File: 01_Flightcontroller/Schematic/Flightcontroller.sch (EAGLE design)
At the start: 86 parts, among them IC1 FT232RL, IC2 MPU6000, IC3 BMP280, J1 2908-05WB-MG, U1 STM32F7X2RXT, U2 ATMEGA328P_TQFP, U3 LM3940IMPX-3.3/NOPB, U4 TXB0104, Y1 8MHz, Y2 16MHz

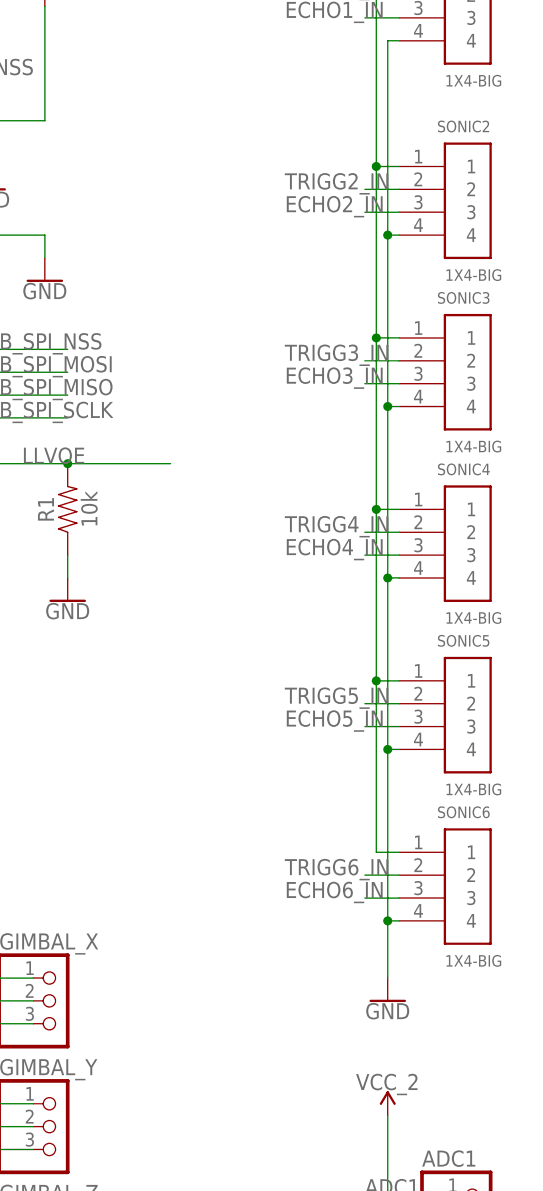
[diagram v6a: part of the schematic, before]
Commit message: Löschen von ünnötigen Pins
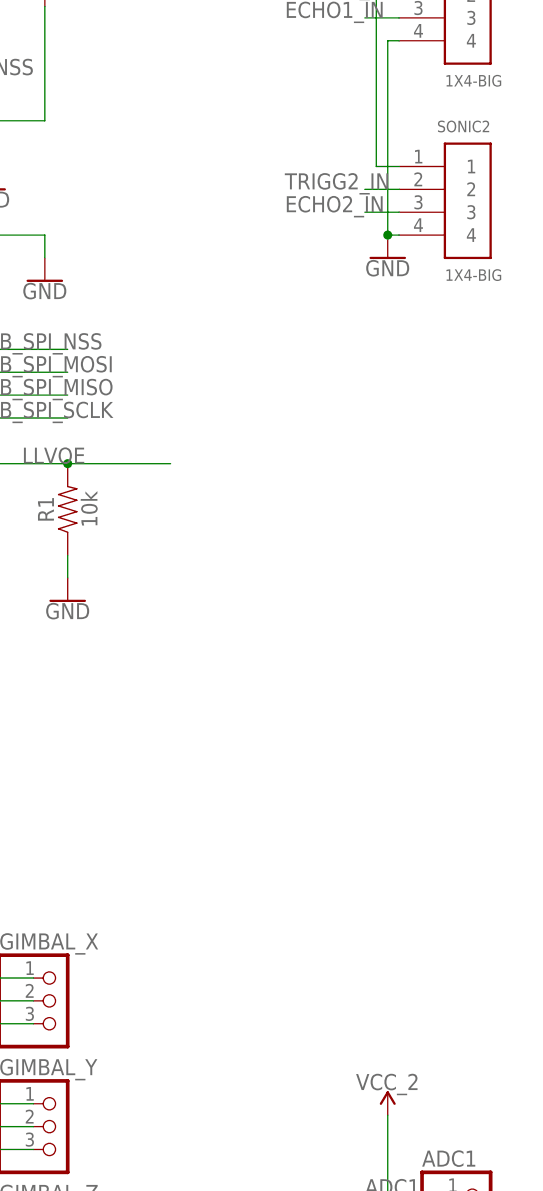
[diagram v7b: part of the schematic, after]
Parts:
- removed SONIC3, SONIC4, SONIC5, SONIC6: 1X4-BIG, adafruit:1X4-BIG
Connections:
- net ECHO3_IN: no longer SONIC3.3
- net ECHO4_IN: no longer SONIC4.3
- net ECHO5_IN: no longer SONIC5.3
- net ECHO6_IN: no longer SONIC6.3
- net GND: no longer SONIC3.4, SONIC4.4, SONIC5.4, SONIC6.4
- net TRIGG3_IN: no longer SONIC3.2
- net TRIGG4_IN: no longer SONIC4.2
- net TRIGG5_IN: no longer SONIC5.2
- net TRIGG6_IN: no longer SONIC6.2
- net VCC_2: no longer SONIC3.1, SONIC4.1, SONIC5.1, SONIC6.1
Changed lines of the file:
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@@
 <?xml version="1.0" encoding="utf-8"?>
 <!DOCTYPE eagle SYSTEM "eagle.dtd">
-<eagle version="9.3.2">
+<eagle version="9.1.3">
 <drawing>
 <settings>
@@
 <part name="SONIC1" library="adafruit" library_urn="urn:adsk.eagle:library:420" deviceset="1X4" device="-BIG" package3d_urn="urn:adsk.eagle:package:6240658/1"/>
 <part name="SONIC2" library="adafruit" library_urn="urn:adsk.eagle:library:420" deviceset="1X4" device="-BIG" package3d_urn="urn:adsk.eagle:package:6240658/1"/>
-<part name="SONIC3" library="adafruit" library_urn="urn:adsk.eagle:library:420" deviceset="1X4" device="-BIG" package3d_urn="urn:adsk.eagle:package:6240658/1"/>
-<part name="SONIC4" library="adafruit" library_urn="urn:adsk.eagle:library:420" deviceset="1X4" device="-BIG" package3d_urn="urn:adsk.eagle:package:6240658/1"/>
-<part name="SONIC5" library="adafruit" library_urn="urn:adsk.eagle:library:420" deviceset="1X4" device="-BIG" package3d_urn="urn:adsk.eagle:package:6240658/1"/>
-<part name="SONIC6" library="adafruit" library_urn="urn:adsk.eagle:library:420" deviceset="1X4" device="-BIG" package3d_urn="urn:adsk.eagle:package:6240658/1"/>
 <part name="SUPPLY22" library="SparkFun-PowerSymbols" library_urn="urn:adsk.eagle:library:530" deviceset="VCC_2" device=""/>
 <part name="GND21" library="SparkFun-PowerSymbols" library_urn="urn:adsk.eagle:library:530" deviceset="GND" device=""/>
@@
 <attribute name="VALUE" x="369.57" y="40.64" size="1.27" layer="96" font="vector"/>
 </instance>
-<instance part="SONIC3" gate="G$1" x="369.57" y="31.75" smashed="yes">
-<attribute name="NAME" x="374.65" y="39.37" size="1.27" layer="95" font="vector" rot="R180"/>
-<attribute name="VALUE" x="369.57" y="21.59" size="1.27" layer="96" font="vector"/>
-</instance>
-<instance part="SONIC4" gate="G$1" x="369.57" y="12.7" smashed="yes">
-<attribute name="NAME" x="374.65" y="20.32" size="1.27" layer="95" font="vector" rot="R180"/>
-<attribute name="VALUE" x="369.57" y="2.54" size="1.27" layer="96" font="vector"/>
-</instance>
-<instance part="SONIC5" gate="G$1" x="369.57" y="-6.35" smashed="yes">
-<attribute name="NAME" x="374.65" y="1.27" size="1.27" layer="95" font="vector" rot="R180"/>
-<attribute name="VALUE" x="369.57" y="-16.51" size="1.27" layer="96" font="vector"/>
-</instance>
-<instance part="SONIC6" gate="G$1" x="369.57" y="-25.4" smashed="yes">
-<attribute name="NAME" x="374.65" y="-17.78" size="1.27" layer="95" font="vector" rot="R180"/>
-<attribute name="VALUE" x="369.57" y="-35.56" size="1.27" layer="96" font="vector"/>
-</instance>
 <instance part="SUPPLY22" gate="G$1" x="361.95" y="82.55" smashed="yes">
 <attribute name="VALUE" x="361.95" y="85.344" size="1.778" layer="96" align="bottom-center"/>
 </instance>
-<instance part="GND21" gate="1" x="363.22" y="-39.37" smashed="yes">
-<attribute name="VALUE" x="363.22" y="-39.624" size="1.778" layer="96" align="top-center"/>
+<instance part="GND21" gate="1" x="363.22" y="43.18" smashed="yes">
+<attribute name="VALUE" x="363.22" y="42.926" size="1.778" layer="96" align="top-center"/>
 </instance>
 <instance part="C31" gate="G$1" x="102.87" y="7.62" smashed="yes" rot="R270">
@@
 </segment>
 <segment>
-<pinref part="SONIC1" gate="G$1" pin="4"/>
-<wire x1="364.49" y1="67.31" x2="363.22" y2="67.31" width="0.1524" layer="91"/>
-<pinref part="SONIC2" gate="G$1" pin="4"/>
-<wire x1="363.22" y1="67.31" x2="363.22" y2="45.72" width="0.1524" layer="91"/>
-<wire x1="363.22" y1="45.72" x2="364.49" y2="45.72" width="0.1524" layer="91"/>
-<pinref part="SONIC3" gate="G$1" pin="4"/>
-<wire x1="363.22" y1="45.72" x2="363.22" y2="26.67" width="0.1524" layer="91"/>
-<wire x1="363.22" y1="26.67" x2="364.49" y2="26.67" width="0.1524" layer="91"/>
-<junction x="363.22" y="45.72"/>
-<pinref part="SONIC4" gate="G$1" pin="4"/>
-<wire x1="363.22" y1="26.67" x2="363.22" y2="7.62" width="0.1524" layer="91"/>
-<wire x1="363.22" y1="7.62" x2="364.49" y2="7.62" width="0.1524" layer="91"/>
-<junction x="363.22" y="26.67"/>
-<pinref part="SONIC5" gate="G$1" pin="4"/>
-<wire x1="363.22" y1="7.62" x2="363.22" y2="-11.43" width="0.1524" layer="91"/>
-<wire x1="363.22" y1="-11.43" x2="364.49" y2="-11.43" width="0.1524" layer="91"/>
-<junction x="363.22" y="7.62"/>
-<pinref part="SONIC6" gate="G$1" pin="4"/>
-<wire x1="363.22" y1="-11.43" x2="363.22" y2="-30.48" width="0.1524" layer="91"/>
-<wire x1="363.22" y1="-30.48" x2="364.49" y2="-30.48" width="0.1524" layer="91"/>
-<junction x="363.22" y="-11.43"/>
-<wire x1="363.22" y1="-30.48" x2="363.22" y2="-36.83" width="0.1524" layer="91"/>
-<junction x="363.22" y="-30.48"/>
-<pinref part="GND21" gate="1" pin="GND"/>
-</segment>
-<segment>
 <pinref part="ADC1" gate="A" pin="3"/>
 <wire x1="370.84" y1="-66.04" x2="364.49" y2="-66.04" width="0.1524" layer="91"/>
@@
 <wire x1="195.58" y1="-1.27" x2="195.58" y2="-3.81" width="0.1524" layer="91"/>
 <pinref part="GND31" gate="1" pin="GND"/>
+</segment>
+<segment>
+<pinref part="SONIC1" gate="G$1" pin="4"/>
+<wire x1="364.49" y1="67.31" x2="363.22" y2="67.31" width="0.1524" layer="91"/>
+<pinref part="SONIC2" gate="G$1" pin="4"/>
+<wire x1="363.22" y1="67.31" x2="363.22" y2="45.72" width="0.1524" layer="91"/>
+<wire x1="363.22" y1="45.72" x2="364.49" y2="45.72" width="0.1524" layer="91"/>
+<pinref part="GND21" gate="1" pin="GND"/>
+<junction x="363.22" y="45.72"/>
 </segment>
 </net>
@@
 </segment>
 <segment>
-<pinref part="SONIC5" gate="G$1" pin="1"/>
-<wire x1="364.49" y1="-3.81" x2="361.95" y2="-3.81" width="0.1524" layer="91"/>
-<wire x1="361.95" y1="-3.81" x2="361.95" y2="-22.86" width="0.1524" layer="91"/>
-<pinref part="SONIC6" gate="G$1" pin="1"/>
-<wire x1="361.95" y1="-22.86" x2="364.49" y2="-22.86" width="0.1524" layer="91"/>
-<pinref part="SONIC4" gate="G$1" pin="1"/>
-<wire x1="364.49" y1="15.24" x2="361.95" y2="15.24" width="0.1524" layer="91"/>
-<wire x1="361.95" y1="15.24" x2="361.95" y2="-3.81" width="0.1524" layer="91"/>
-<junction x="361.95" y="-3.81"/>
-<pinref part="SONIC3" gate="G$1" pin="1"/>
-<wire x1="361.95" y1="15.24" x2="361.95" y2="34.29" width="0.1524" layer="91"/>
-<wire x1="361.95" y1="34.29" x2="364.49" y2="34.29" width="0.1524" layer="91"/>
-<junction x="361.95" y="15.24"/>
 <pinref part="SONIC2" gate="G$1" pin="1"/>
-<wire x1="361.95" y1="34.29" x2="361.95" y2="53.34" width="0.1524" layer="91"/>
 <wire x1="361.95" y1="53.34" x2="364.49" y2="53.34" width="0.1524" layer="91"/>
-<junction x="361.95" y="34.29"/>
 <pinref part="SONIC1" gate="G$1" pin="1"/>
 <wire x1="361.95" y1="53.34" x2="361.95" y2="74.93" width="0.1524" layer="91"/>
 <wire x1="361.95" y1="74.93" x2="364.49" y2="74.93" width="0.1524" layer="91"/>
-<junction x="361.95" y="53.34"/>
 <wire x1="361.95" y1="74.93" x2="361.95" y2="82.55" width="0.1524" layer="91"/>
 <junction x="361.95" y="74.93"/>
@@
 <label x="213.36" y="72.39" size="1.778" layer="95"/>
 </segment>
-<segment>
-<pinref part="SONIC3" gate="G$1" pin="2"/>
-<wire x1="364.49" y1="31.75" x2="360.68" y2="31.75" width="0.1524" layer="91"/>
-<label x="351.79" y="31.75" size="1.778" layer="95"/>
-</segment>
 </net>
 <net name="ECHO3_IN" class="0">
@@
 <label x="213.36" y="69.85" size="1.778" layer="95"/>
 </segment>
-<segment>
-<pinref part="SONIC3" gate="G$1" pin="3"/>
-<wire x1="364.49" y1="29.21" x2="360.68" y2="29.21" width="0.1524" layer="91"/>
-<label x="351.79" y="29.21" size="1.778" layer="95"/>
-</segment>
 </net>
 <net name="TRIGG4_IN" class="0">
@@
 <label x="213.36" y="46.99" size="1.778" layer="95"/>
 </segment>
-<segment>
-<pinref part="SONIC4" gate="G$1" pin="2"/>
-<wire x1="364.49" y1="12.7" x2="360.68" y2="12.7" width="0.1524" layer="91"/>
-<label x="351.79" y="12.7" size="1.778" layer="95"/>
-</segment>
 </net>
 <net name="ECHO4_IN" class="0">
@@
 <label x="213.36" y="44.45" size="1.778" layer="95"/>
 </segment>
-<segment>
-<pinref part="SONIC4" gate="G$1" pin="3"/>
-<wire x1="364.49" y1="10.16" x2="360.68" y2="10.16" width="0.1524" layer="91"/>
-<label x="351.79" y="10.16" size="1.778" layer="95"/>
-</segment>
 </net>
 <net name="TRIGG5_IN" class="0">
@@
 <label x="213.36" y="41.91" size="1.778" layer="95"/>
 </segment>
-<segment>
-<pinref part="SONIC5" gate="G$1" pin="2"/>
-<wire x1="364.49" y1="-6.35" x2="360.68" y2="-6.35" width="0.1524" layer="91"/>
-<label x="351.79" y="-6.35" size="1.778" layer="95"/>
-</segment>
 </net>
 <net name="ECHO5_IN" class="0">
@@
 <label x="213.36" y="39.37" size="1.778" layer="95"/>
 </segment>
-<segment>
-<pinref part="SONIC5" gate="G$1" pin="3"/>
-<wire x1="364.49" y1="-8.89" x2="360.68" y2="-8.89" width="0.1524" layer="91"/>
-<label x="351.79" y="-8.89" size="1.778" layer="95"/>
-</segment>
 </net>
 <net name="TRIGG6_IN" class="0">
@@
 <label x="213.36" y="36.83" size="1.778" layer="95"/>
 </segment>
-<segment>
-<pinref part="SONIC6" gate="G$1" pin="2"/>
-<wire x1="364.49" y1="-25.4" x2="360.68" y2="-25.4" width="0.1524" layer="91"/>
-<label x="351.79" y="-25.4" size="1.778" layer="95"/>
-</segment>
 </net>
 <net name="ECHO6_IN" class="0">
@@
 <label x="213.36" y="31.75" size="1.778" layer="95"/>
 </segment>
-<segment>
-<pinref part="SONIC6" gate="G$1" pin="3"/>
-<wire x1="364.49" y1="-27.94" x2="360.68" y2="-27.94" width="0.1524" layer="91"/>
-<label x="351.79" y="-27.94" size="1.778" layer="95"/>
-</segment>
-</net>
+</net>

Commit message: Versuchen vom routen 143Vias -> 143 Sorgetelefon :).
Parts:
- added JP1, JP2, JP3, JP4, JP5, JP6, JP7: (no value), adafruit:PINHD-1X6
- C1, C13, C2, C20, C21, C27: device resistor:C-EUC1206 -> resistor:C-EUC0805
- C10, C11, C8, C9: device rcl:C-EUC1808 -> rcl:C-EUC0805
- C12, C14, C15, C16, C17, C18, C19, C23, C24, C25, C26, C28, C29, C3, C30, C31, C34, C35, C4, C5, C6, C7: device rcl:C-EUC1206 -> rcl:C-EUC0805
- C22, C32, C33: device rcl:C-EUC1812 -> rcl:C-EUC0805
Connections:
- net VCC: no longer M1.2, M2.2, M3.2, M4.2
- net VCC_2: now also M1.2, M2.2, M3.2, M4.2
